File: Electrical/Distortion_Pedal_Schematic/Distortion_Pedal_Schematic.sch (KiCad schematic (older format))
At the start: 28 parts

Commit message: Initial Schematic
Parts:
- C? (x2): value C -> 47u
- C?: value C -> 1n
- C? (x4): value C -> 1u
- R? (x2): value R -> 1M
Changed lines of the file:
@@
 P 1925 2575
 F 0 "C?" V 1673 2575 50  0000 C CNN
-F 1 "C" V 1764 2575 50  0000 C CNN
+F 1 "47u" V 1764 2575 50  0000 C CNN
 F 2 "" H 1963 2425 50  0001 C CNN
 F 3 "~" H 1925 2575 50  0001 C CNN
@@
 P 5950 3500
 F 0 "C?" H 6065 3546 50  0000 L CNN
-F 1 "C" H 6065 3455 50  0000 L CNN
+F 1 "1n" H 6065 3455 50  0000 L CNN
 F 2 "" H 5988 3350 50  0001 C CNN
 F 3 "~" H 5950 3500 50  0001 C CNN
@@
 P 7625 2425
 F 0 "C?" V 7373 2425 50  0000 C CNN
-F 1 "C" V 7464 2425 50  0000 C CNN
+F 1 "47u" V 7464 2425 50  0000 C CNN
 F 2 "" H 7663 2275 50  0001 C CNN
 F 3 "~" H 7625 2425 50  0001 C CNN
@@
 P 5125 5525
 F 0 "C?" H 5240 5571 50  0000 L CNN
-F 1 "C" H 5240 5480 50  0000 L CNN
+F 1 "1u" H 5240 5480 50  0000 L CNN
 F 2 "" H 5163 5375 50  0001 C CNN
 F 3 "~" H 5125 5525 50  0001 C CNN
@@
 P 6350 5500
 F 0 "C?" H 6465 5546 50  0000 L CNN
-F 1 "C" H 6465 5455 50  0000 L CNN
+F 1 "1u" H 6465 5455 50  0000 L CNN
 F 2 "" H 6388 5350 50  0001 C CNN
 F 3 "~" H 6350 5500 50  0001 C CNN
@@
 P 8575 5000
 F 0 "R?" H 8505 4954 50  0000 R CNN
-F 1 "R" H 8505 5045 50  0000 R CNN
+F 1 "1M" H 8505 5045 50  0000 R CNN
 F 2 "" V 8505 5000 50  0001 C CNN
 F 3 "~" H 8575 5000 50  0001 C CNN
@@
 P 8575 5600
 F 0 "R?" H 8505 5554 50  0000 R CNN
-F 1 "R" H 8505 5645 50  0000 R CNN
+F 1 "1M" H 8505 5645 50  0000 R CNN
 F 2 "" V 8505 5600 50  0001 C CNN
 F 3 "~" H 8575 5600 50  0001 C CNN
@@
 P 9000 5000
 F 0 "C?" H 9115 5046 50  0000 L CNN
-F 1 "C" H 9115 4955 50  0000 L CNN
+F 1 "1u" H 9115 4955 50  0000 L CNN
 F 2 "" H 9038 4850 50  0001 C CNN
 F 3 "~" H 9000 5000 50  0001 C CNN
@@
 P 9000 5600
 F 0 "C?" H 9115 5646 50  0000 L CNN
-F 1 "C" H 9115 5555 50  0000 L CNN
+F 1 "1u" H 9115 5555 50  0000 L CNN
 F 2 "" H 9038 5450 50  0001 C CNN
 F 3 "~" H 9000 5600 50  0001 C CNN

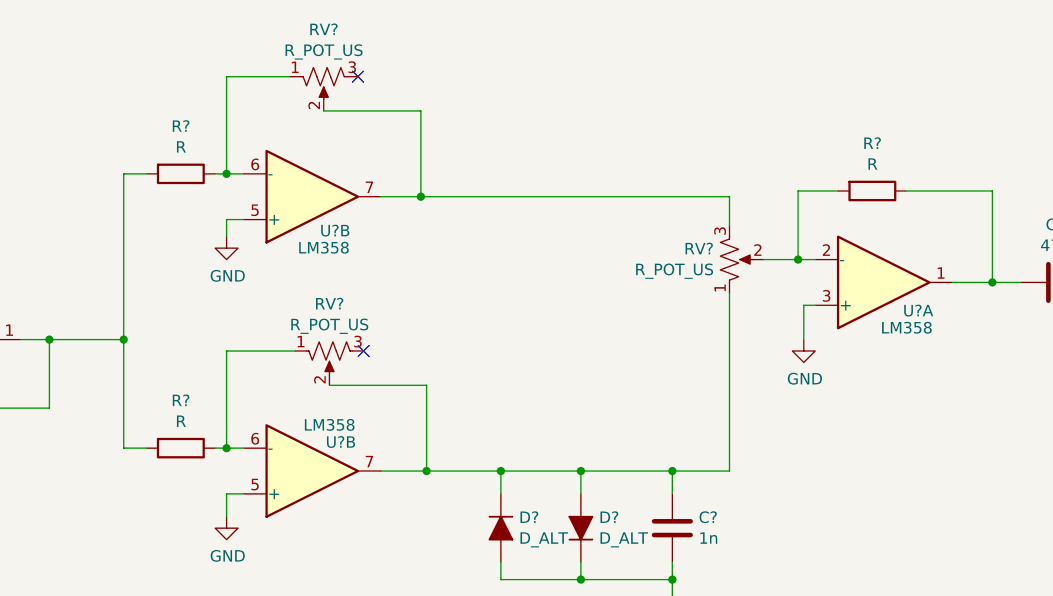
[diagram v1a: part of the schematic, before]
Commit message: Added simulation and changed to soft clipping
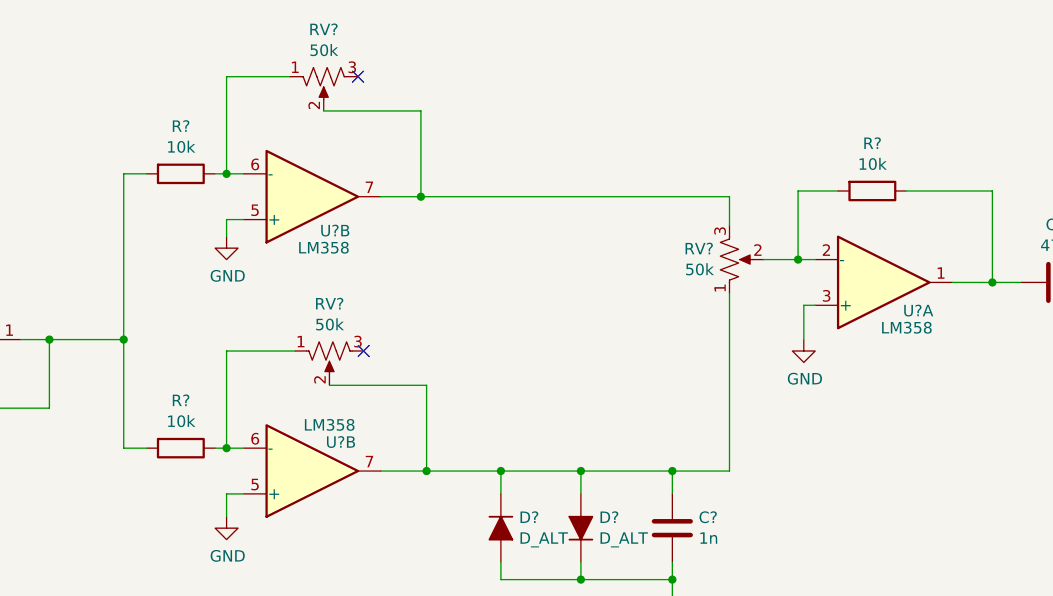
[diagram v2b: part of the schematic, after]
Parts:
- R? (x3): value R -> 10k
- RV? (x3): value R_POT_US -> 50k
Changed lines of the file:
@@
 EESchema Schematic File Version 4
+LIBS:Distortion_Pedal_Schematic-cache
 EELAYER 26 0
 EELAYER END
@@
 P 3800 1950
 F 0 "R?" V 3593 1950 50  0000 C CNN
-F 1 "R" V 3684 1950 50  0000 C CNN
+F 1 "10k" V 3684 1950 50  0000 C CNN
 F 2 "" V 3730 1950 50  0001 C CNN
 F 3 "~" H 3800 1950 50  0001 C CNN
@@
 P 3800 3150
 F 0 "R?" V 3593 3150 50  0000 C CNN
-F 1 "R" V 3684 3150 50  0000 C CNN
+F 1 "10k" V 3684 3150 50  0000 C CNN
 F 2 "" V 3730 3150 50  0001 C CNN
 F 3 "~" H 3800 3150 50  0001 C CNN
@@
 P 4450 2725
 F 0 "RV?" V 4245 2725 50  0000 C CNN
-F 1 "R_POT_US" V 4336 2725 50  0000 C CNN
+F 1 "50k" V 4336 2725 50  0000 C CNN
 F 2 "" H 4450 2725 50  0001 C CNN
 F 3 "~" H 4450 2725 50  0001 C CNN
@@
 P 6825 2025
 F 0 "R?" V 6618 2025 50  0000 C CNN
-F 1 "R" V 6709 2025 50  0000 C CNN
+F 1 "10k" V 6709 2025 50  0000 C CNN
 F 2 "" V 6755 2025 50  0001 C CNN
 F 3 "~" H 6825 2025 50  0001 C CNN
@@
 P 6200 2325
 F 0 "RV?" H 6132 2279 50  0000 R CNN
-F 1 "R_POT_US" H 6132 2370 50  0000 R CNN
+F 1 "50k" H 6132 2370 50  0000 R CNN
 F 2 "" H 6200 2325 50  0001 C CNN
 F 3 "~" H 6200 2325 50  0001 C CNN
@@
 P 4425 1525
 F 0 "RV?" V 4220 1525 50  0000 C CNN
-F 1 "R_POT_US" V 4311 1525 50  0000 C CNN
+F 1 "50k" V 4311 1525 50  0000 C CNN
 F 2 "" H 4425 1525 50  0001 C CNN
 F 3 "~" H 4425 1525 50  0001 C CNN

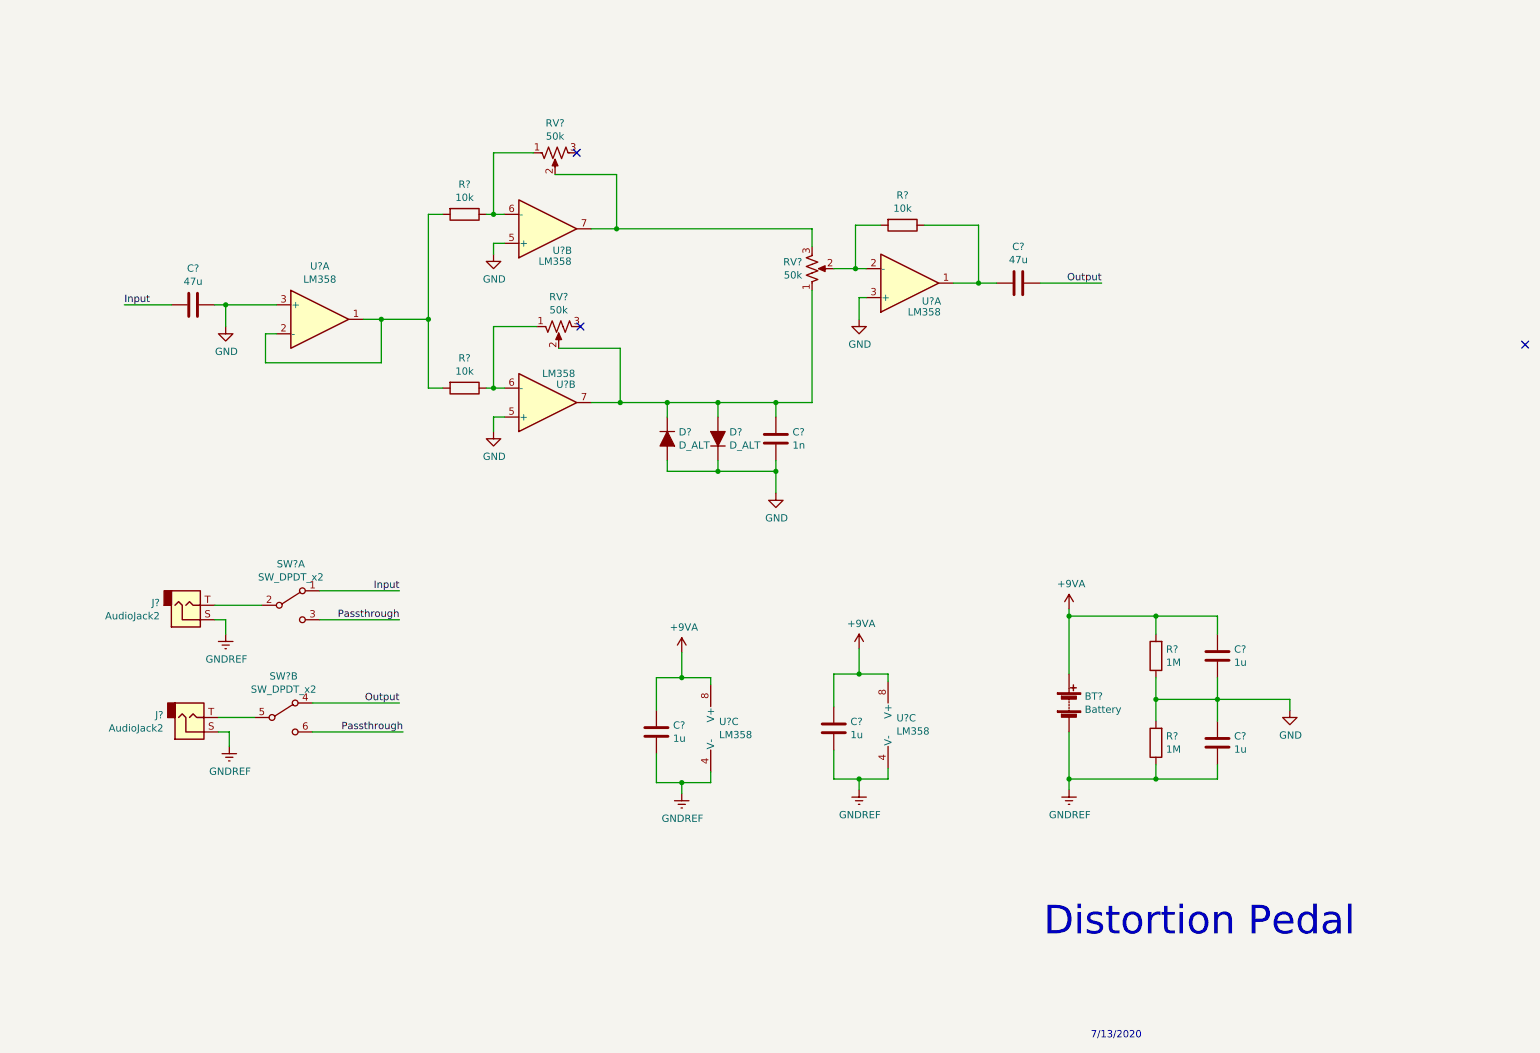
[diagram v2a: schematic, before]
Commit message: Changed BalanceAmplifier
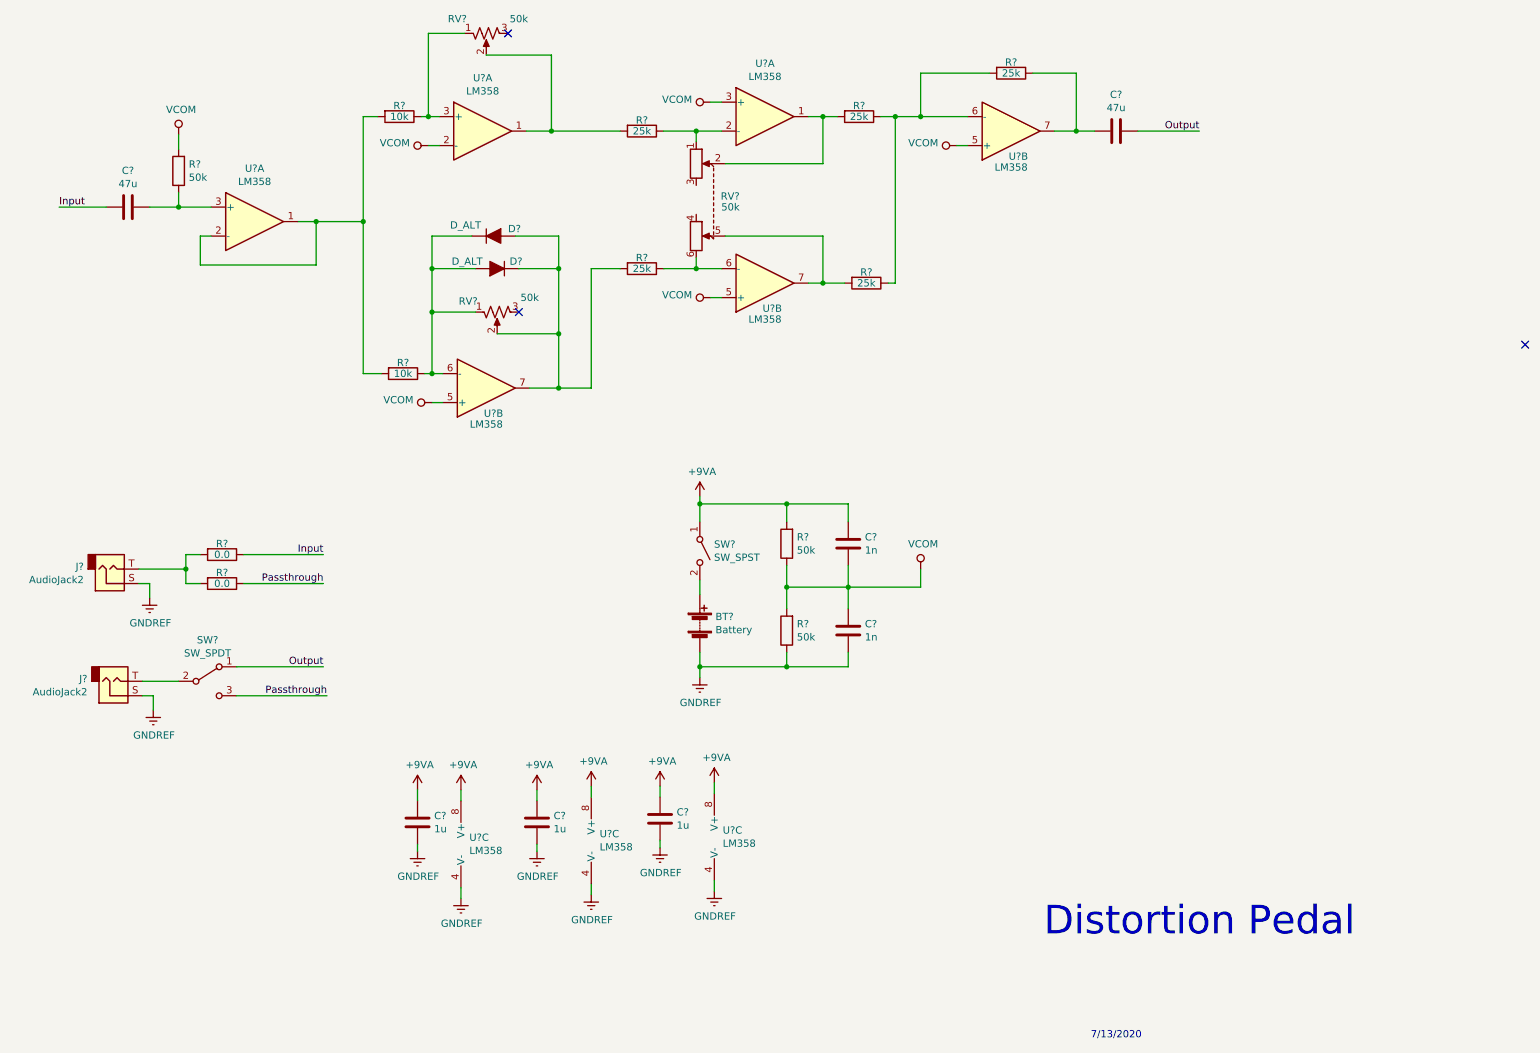
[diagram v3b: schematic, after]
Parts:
- removed C?: 1n, symbol Device:C
- removed C?: 1u, symbol Device:C
- removed D?: D_ALT, symbol Device:D_ALT
- removed R?: 10k, symbol Device:R
- removed RV?: 50k, symbol Device:R_POT_US
- removed SW? (x2): SW_DPDT_x2, symbol Switch:SW_DPDT_x2
- removed U? (x4): LM358, symbol Amplifier_Operational:LM358
- added C? (x2): 1u, symbol Device:C
- added D?: D_ALT, symbol Device:D_ALT
- added R? (x2): 0.0, symbol Device:R
- added R? (x5): 25k, symbol Device:R
- added R?: 50k, symbol Device:R
- added RV?: 50k, symbol Device:R_POT_Dual
- added SW?: SW_SPDT, symbol Switch:SW_SPDT
- added SW?: SW_SPST, symbol Switch:SW_SPST
- added U? (x7): LM358, symbol Amplifier_Operational:LM358
- C? (x2): value 1u -> 1n
- R? (x2): value 1M -> 50k
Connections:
- net +9VA: now also C?.1, C?.1, SW?.1 (A), U?.8 (V+); no longer BT?.1 (+)
- net GNDREF: now also C?.2, C?.2, U?.4 (V-)
- net Input: now also R?.1
- net Output: now also SW?.1 (A)
- net Passthrough: now also R?.1, SW?.3 (C)
- net at J?.T: now also R?.2, R?.2
- net at R?.2, R?.2: now also U?.1, U?.2 (-)
- net at R?.1, RV?.1: now also U?.3 (+)
- net at RV?.2: now also R?.2, U?.1
- net at C?.2: now also R?.1, U?.7
- net at R?.1, RV?.1: now also D?.2 (A), D?.1 (K), U?.6 (-)
- net at D?.1 (K), RV?.2: now also D?.2 (A), R?.2, U?.7
- net at J?.T: now also SW?.2 (B)
- net GND renamed VCOM
- net VCOM: now also R?.2, U?.2 (-), U?.3 (+), U?.5 (+), U?.5 (+), U?.5 (+); no longer C?.1, D?.2 (A)
- new net: C?.1, R?.1, U?.3 (+)
- new net: BT?.1 (+), SW?.2 (B)
- new net: R?.1, RV?.1, U?.2 (-)
- new net: R?.2, RV?.2, U?.1
- new net: R?.2, RV?.5, U?.7
- new net: R?.1, RV?.6, U?.6 (-)
- new net: R?.1, R?.1, R?.2, U?.6 (-)
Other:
- moved on the sheet: BT?, C?, D?, J?, R?, RV?, U?C

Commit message: Removed simulation
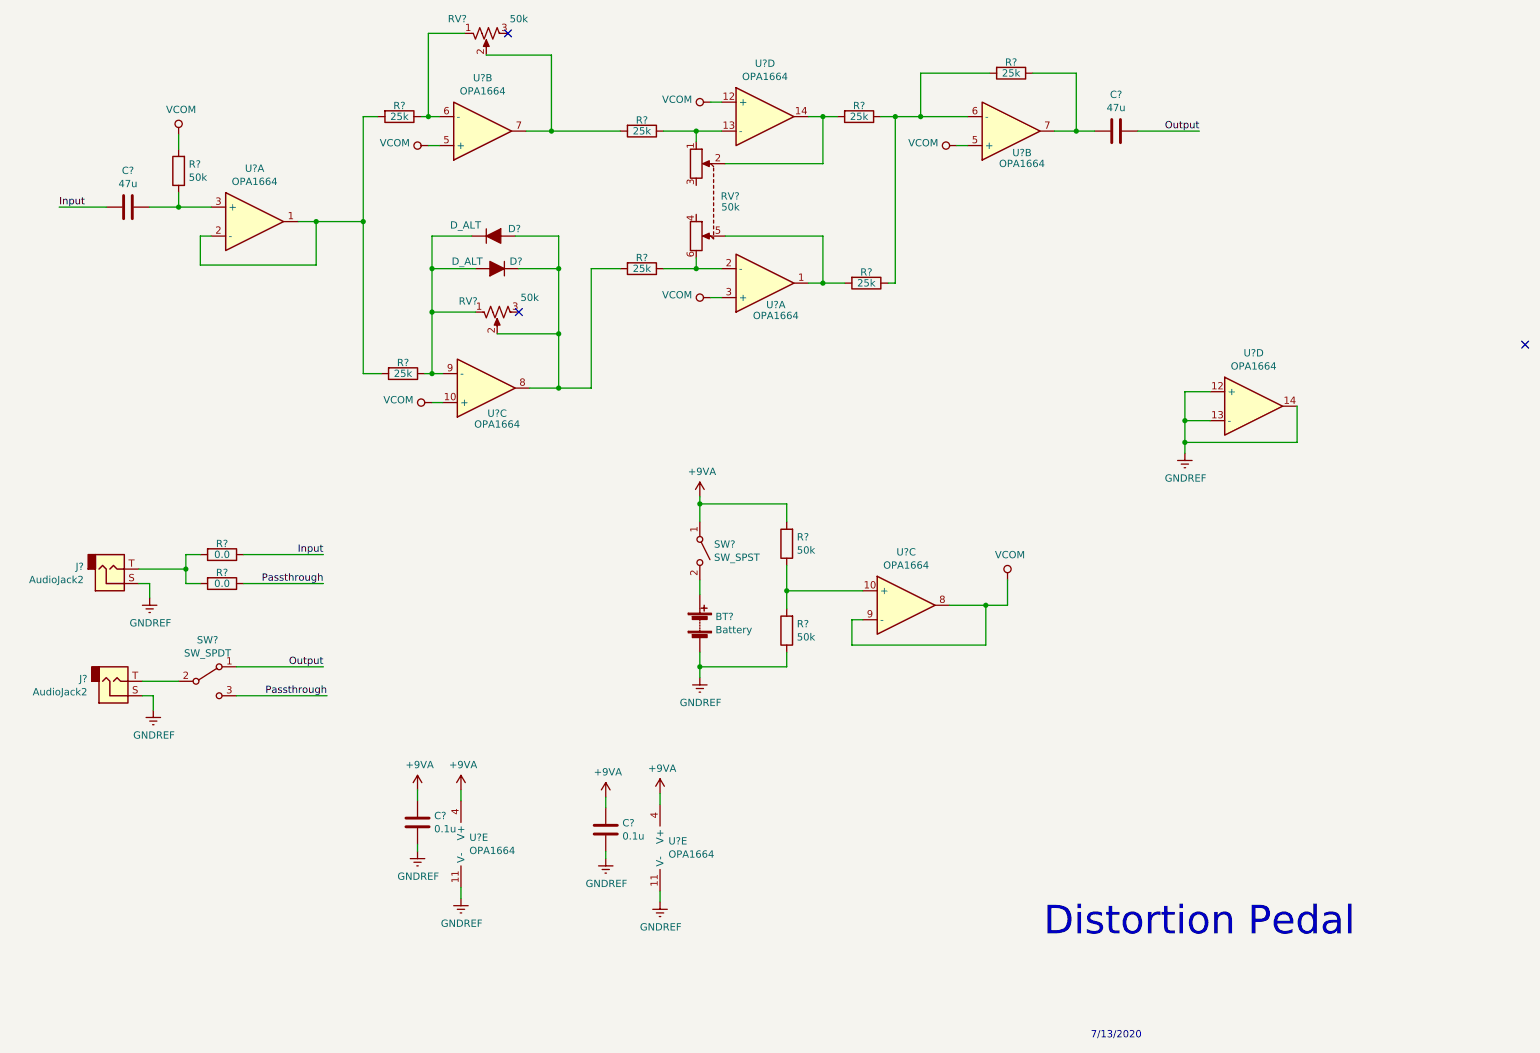
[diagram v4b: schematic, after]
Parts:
- removed C? (x2): 1n, symbol Device:C
- removed C?: 1u, symbol Device:C
- removed U? (x9): LM358, symbol Amplifier_Operational:LM358
- added U? (x10): OPA1664, symbol Device:Opamp_Quad_Generic
- C? (x2): value 1u -> 0.1u
- R? (x2): value 10k -> 25k
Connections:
- net +9VA: now also U?.4 (V+), U?.4 (V+)
- net GNDREF: now also U?.11 (V-), U?.11 (V-), U?.12 (+), U?.13 (-), U?.14
- net VCOM: now also U?.10 (+), U?.12 (+), U?.3 (+), U?.5 (+), U?.5 (+), U?.8, U?.9 (-); no longer R?.1, R?.2
- net at C?.1, R?.1: now also U?.3 (+)
- net at R?.1, RV?.1: now also U?.6 (-)
- net at R?.2, R?.2: now also U?.1, U?.2 (-)
- net at D?.1 (K), D?.2 (A), R?.1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: now also U?.9 (-)
- net at D?.1 (K), D?.2 (A), R?.2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: now also U?.8
- net at C?.2, R?.1: now also U?.7
- net at R?.2, RV?.2: now also U?.7
- net at R?.1, RV?.1: now also U?.13 (-)
- net at R?.2, RV?.2: now also U?.14
- net at R?.2, RV?.5: now also U?.1
- net at R?.1, RV?.6: now also U?.2 (-)
- net at R?.1, R?.1, R?.2: now also U?.6 (-)
- new net: R?.1, R?.2, U?.10 (+)
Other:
- moved on the sheet: C?

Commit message: Part selection
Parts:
- removed BT?: Battery, symbol Device:Battery
- removed SW?: SW_SPDT, symbol Switch:SW_SPDT
- removed SW?: SW_SPST, symbol Switch:SW_SPST
- removed U? (x10): OPA1664, symbol Device:Opamp_Quad_Generic
- added J2: 9v Battery, symbol Connector:Screw_Terminal_01x02
- added SW1: SW_DPDT, symbol Switch:SW_DPDT_x2
- added U1, U2: OPA1664, symbol Device:Opamp_Quad_Generic
- gave numbers to parts that had none: 23
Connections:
- net +9VA: now also SW1.1 (A), U1.4 (V+), U2.4 (V+)
- net GNDREF: now also J2.2 (Pin_2), U1.11 (V-), U2.10 (+), U2.11 (V-), U2.8, U2.9 (-)
- net Output: now also SW1.4 (A)
- net Passthrough: now also SW1.6 (C)
- net VCOM: now also U1.13 (-), U1.2 (-), U1.9 (-), U2.13 (-), U2.14, U2.3 (+), U2.6 (-)
- net at C2.1, R5.1: now also U1.5 (+)
- net at R2.1, RV1.1: now also U1.3 (+)
- net at R2.2, R8.2: now also U1.6 (-), U1.7
- net at D1.1 (K), D2.2 (A), R8.1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: now also U1.12 (+)
- net at D1.2 (A), D2.1 (K), R6.2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: now also U1.14
- net at J3.T: now also SW1.5 (B)
- net at C1.2, R1.1: now also U2.7
- net at R4.2, RV1.2: now also U1.1
- net at R4.1, RV2.1: now also U2.2 (-)
- net at R3.2, RV2.2: now also U2.1
- net at R7.2, RV2.5: now also U1.8
- net at R6.1, RV2.6: now also U1.10 (+)
- net at R1.2, R3.1, R7.1: now also U2.5 (+)
- net at R12.2, R9.1: now also U2.12 (+)
- new net: J2.1 (Pin_1), SW1.2 (B)
- no-connect marks 3 -> 4
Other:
- moved on the sheet: C3
